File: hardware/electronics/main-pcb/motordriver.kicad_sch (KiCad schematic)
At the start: 0 parts

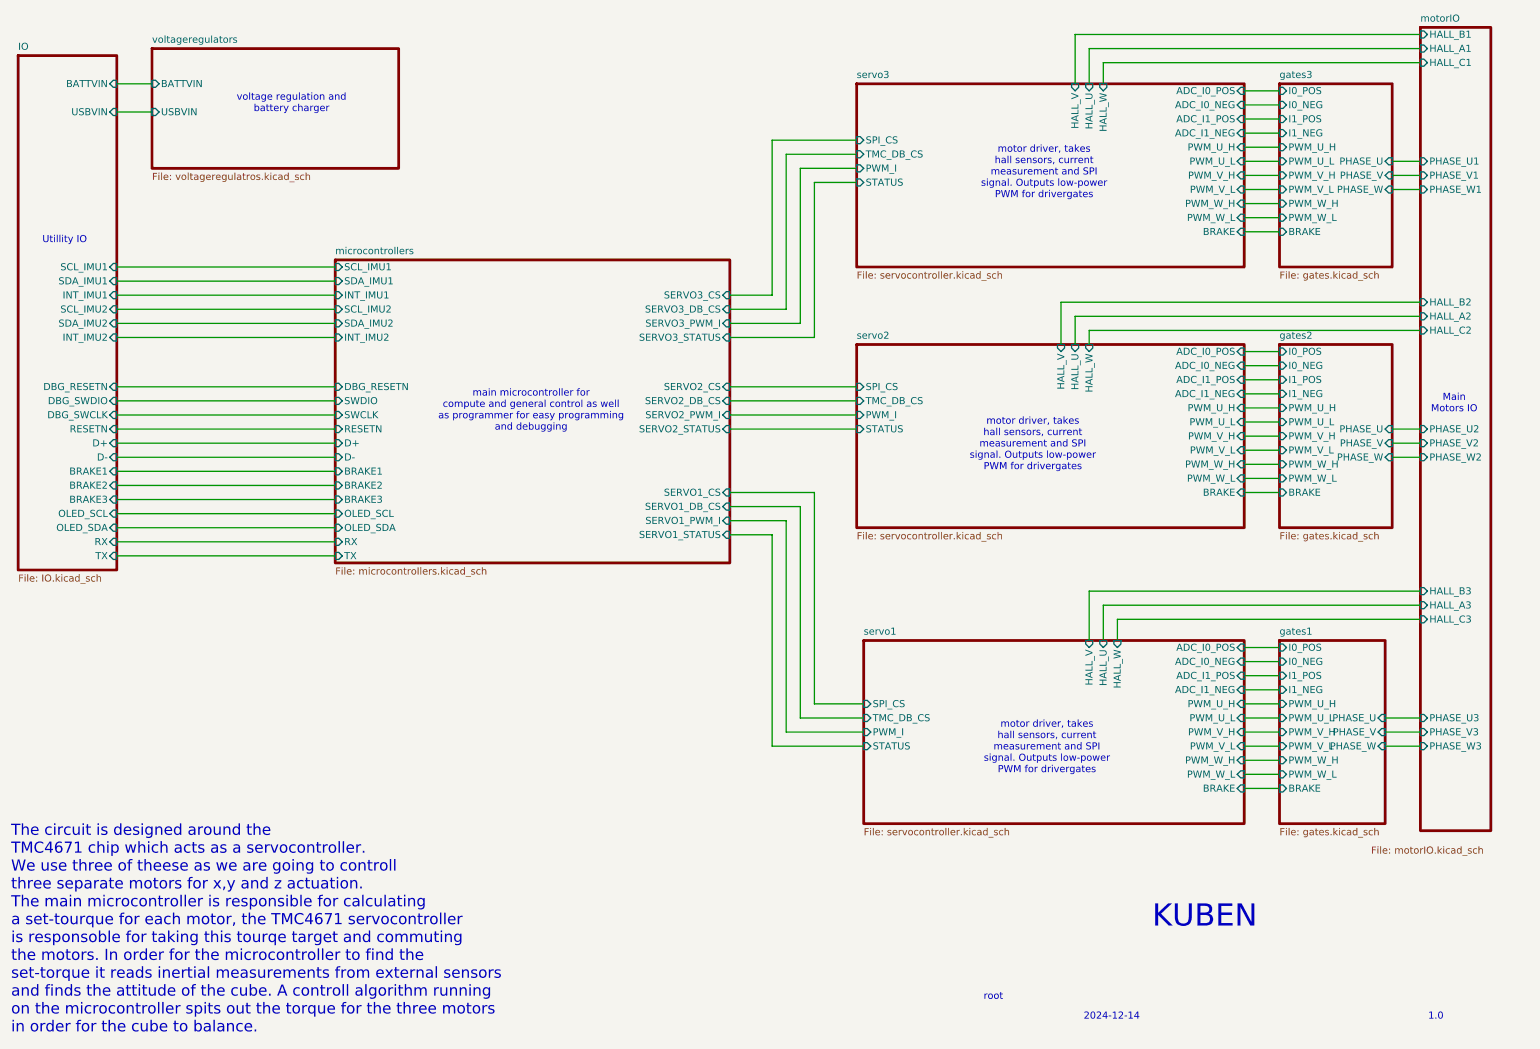
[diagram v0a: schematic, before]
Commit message: added new brake chopper logic, the previous was sketchy, still we might need to find better brake resistors than the one I added
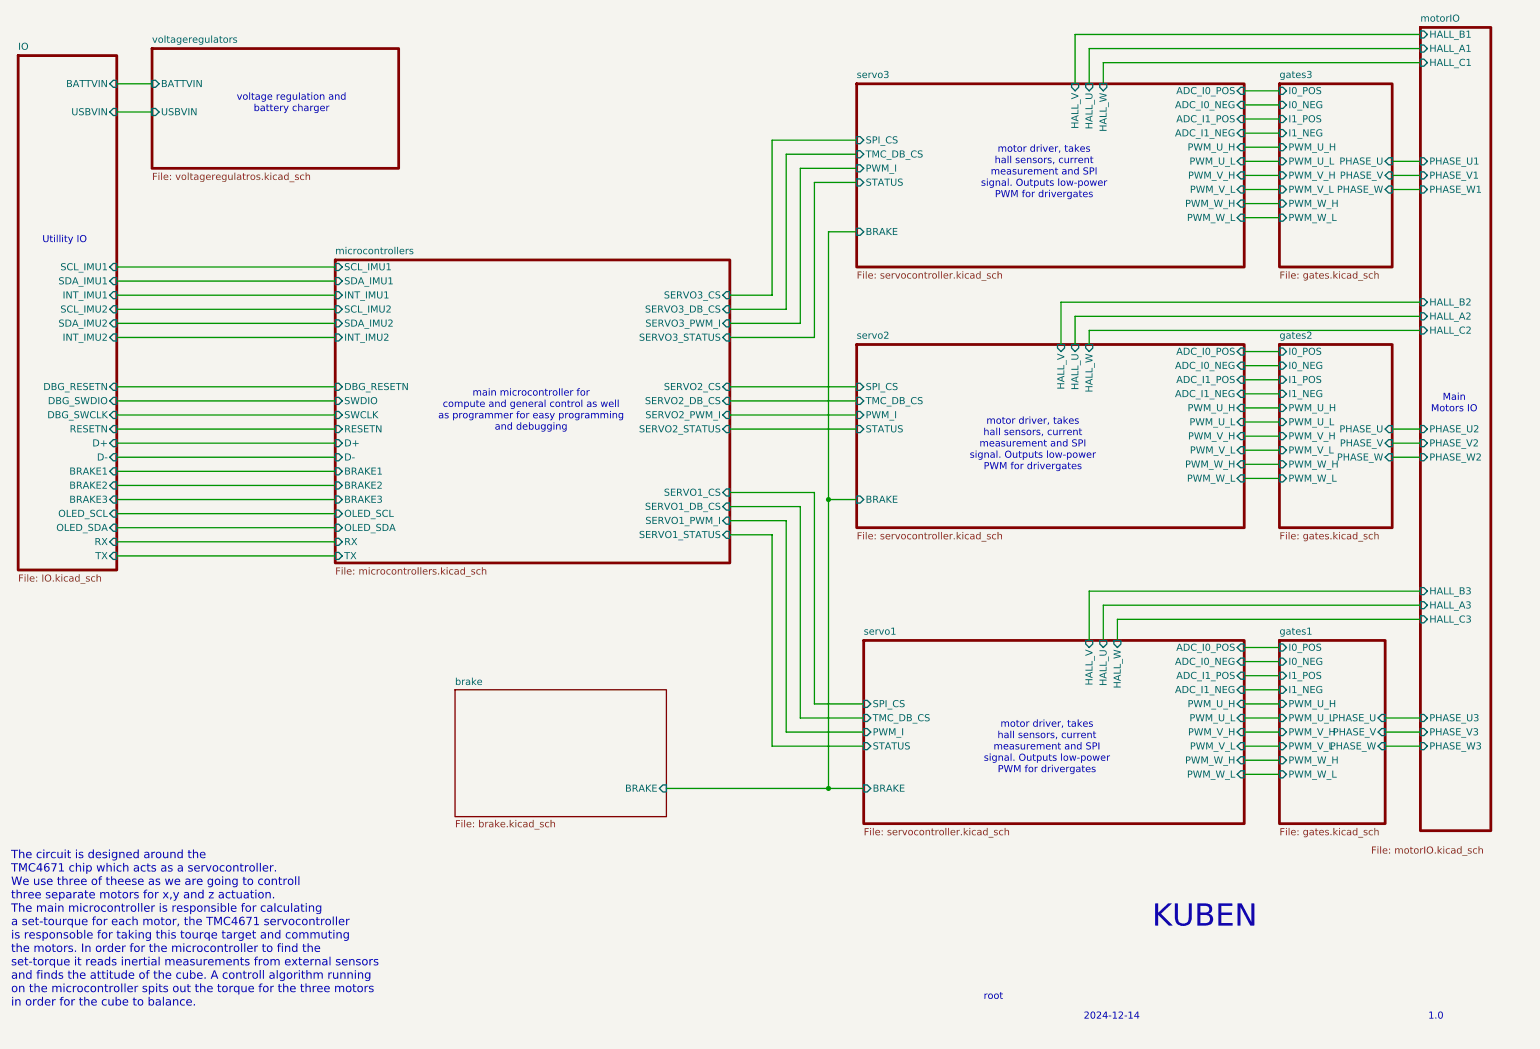
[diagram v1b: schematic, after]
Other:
- added sheet brake (brake.kicad_sch)
- sheet gates1 ports: added none; removed BRAKE
- sheet gates2 ports: added none; removed BRAKE
- sheet gates3 ports: added none; removed BRAKE
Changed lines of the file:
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@@
 	(generator_version "8.0")
 	(paper "A4")
+	(junction
+		(at 161.29 152.4)
+		(diameter 0)
+		(color 0 0 0 0)
+	)
+	(junction
+		(at 161.29 100.33)
+		(diameter 0)
+		(color 0 0 0 0)
+	)
 	(wire
 		(pts
@@
 	(wire
 		(pts
-			(xy 236.22 152.4) (xy 242.57 152.4)
-		)
-		(stroke
-			(width 0)
-			(type default)
-		)
-	)
-	(wire
-		(pts
 			(xy 236.22 139.7) (xy 242.57 139.7)
 		)
@@
 	(wire
 		(pts
+			(xy 161.29 100.33) (xy 166.37 100.33)
+		)
+		(stroke
+			(width 0)
+			(type default)
+		)
+	)
+	(wire
+		(pts
+			(xy 161.29 52.07) (xy 161.29 100.33)
+		)
+		(stroke
+			(width 0)
+			(type default)
+		)
+	)
+	(wire
+		(pts
 			(xy 205.74 16.51) (xy 267.97 16.51)
 		)
@@
 	(wire
 		(pts
+			(xy 132.08 152.4) (xy 161.29 152.4)
+		)
+		(stroke
+			(width 0)
+			(type default)
+		)
+	)
+	(wire
+		(pts
 			(xy 156.21 101.6) (xy 156.21 139.7)
 		)
@@
 	(wire
 		(pts
+			(xy 161.29 100.33) (xy 161.29 152.4)
+		)
+		(stroke
+			(width 0)
+			(type default)
+		)
+	)
+	(wire
+		(pts
 			(xy 236.22 34.29) (xy 242.57 34.29)
 		)
@@
 	(wire
 		(pts
-			(xy 236.22 99.06) (xy 242.57 99.06)
-		)
-		(stroke
-			(width 0)
-			(type default)
-		)
-	)
-	(wire
-		(pts
 			(xy 143.51 66.04) (xy 153.67 66.04)
 		)
@@
 	(wire
 		(pts
-			(xy 236.22 52.07) (xy 242.57 52.07)
-		)
-		(stroke
-			(width 0)
-			(type default)
-		)
-	)
-	(wire
-		(pts
 			(xy 262.89 92.71) (xy 267.97 92.71)
 		)
@@
 	(wire
 		(pts
+			(xy 161.29 152.4) (xy 167.64 152.4)
+		)
+		(stroke
+			(width 0)
+			(type default)
+		)
+	)
+	(wire
+		(pts
 			(xy 236.22 93.98) (xy 242.57 93.98)
+		)
+		(stroke
+			(width 0)
+			(type default)
+		)
+	)
+	(wire
+		(pts
+			(xy 166.37 52.07) (xy 161.29 52.07)
 		)
 		(stroke
@@
 		(effects
 			(font
-				(size 2 2)
+				(size 1.5 1.5)
 			)
 			(justify left)
@@
 		)
 		(pin "BRAKE" input
-			(at 236.22 152.4 0)
-			(effects
-				(font
-					(size 1.27 1.27)
-				)
-				(justify right)
+			(at 167.64 152.4 180)
+			(effects
+				(font
+					(size 1.27 1.27)
+				)
+				(justify left)
 			)
 		)
@@
 		)
 		(pin "BRAKE" input
-			(at 236.22 52.07 0)
-			(effects
-				(font
-					(size 1.27 1.27)
-				)
-				(justify right)
+			(at 166.37 52.07 180)
+			(effects
+				(font
+					(size 1.27 1.27)
+				)
+				(justify left)
 			)
 		)
@@
 			)
 		)
-		(pin "BRAKE" input
-			(at 242.57 52.07 180)
-			(effects
-				(font
-					(size 1.27 1.27)
-				)
-				(justify left)
-			)
-		)
 		(instances
 			(project "motordriver"
@@
 		)
 		(pin "BRAKE" input
-			(at 236.22 99.06 0)
-			(effects
-				(font
-					(size 1.27 1.27)
-				)
-				(justify right)
+			(at 166.37 100.33 180)
+			(effects
+				(font
+					(size 1.27 1.27)
+				)
+				(justify left)
 			)
 		)
@@
 			)
 		)
-		(pin "BRAKE" input
-			(at 242.57 152.4 180)
-			(effects
-				(font
-					(size 1.27 1.27)
-				)
-				(justify left)
-			)
-		)
 		(instances
 			(project "motordriver"
@@
 	)
 	(sheet
+		(at 93.98 134.62)
+		(size 38.1 22.86)
+		(fields_autoplaced yes)
+		(stroke
+			(width 0.1524)
+			(type solid)
+		)
+		(fill
+			(color 0 0 0 0.0000)
+		)
+		(property "Sheetname" "brake"
+			(at 93.98 133.9084 0)
+			(effects
+				(font
+					(size 1.27 1.27)
+				)
+				(justify left bottom)
+			)
+		)
+		(property "Sheetfile" "brake.kicad_sch"
+			(at 93.98 158.0646 0)
+			(effects
+				(font
+					(size 1.27 1.27)
+				)
+				(justify left top)
+			)
+		)
+		(pin "BRAKE" input
+			(at 132.08 152.4 0)
+			(effects
+				(font
+					(size 1.27 1.27)
+				)
+				(justify right)
+			)
+		)
+		(instances
+			(project "motordriver"
+				(path "/c7634e88-16d1-45ec-9aac-9c841e03cf6d"
+					(page "12")
+				)
+			)
+		)
+	)
+	(sheet
 		(at 242.57 72.39)
 		(size 20.32 33.02)
@@
 			(effects
 				(font
-					(size 1.27 1.27)
-				)
-				(justify left)
-			)
-		)
-		(pin "BRAKE" input
-			(at 242.57 99.06 180)
-			(effects
-				(font

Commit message: saved here
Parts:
- added C1: 10µF, Capacitor_SMD:C_0603_1608Metric, symbol Device:C
- added Y1: DSC6001CI2B-025.0000T, kuben-footprints:DSC6001CI2B0250000T, symbol DSC6001CI2B-025_0000T:DSC6001CI2B-025.0000T
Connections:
- new net +3.3V: C1.1, Y1.1 (OE), Y1.4 (VDD)
- new net GND: C1.2, Y1.2 (GND)
- new net SERVO_CLK: Y1.3 (OUT)
